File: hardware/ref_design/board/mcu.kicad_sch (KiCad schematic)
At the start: 8 parts, among them U4 RP2354B, X1 12MHz

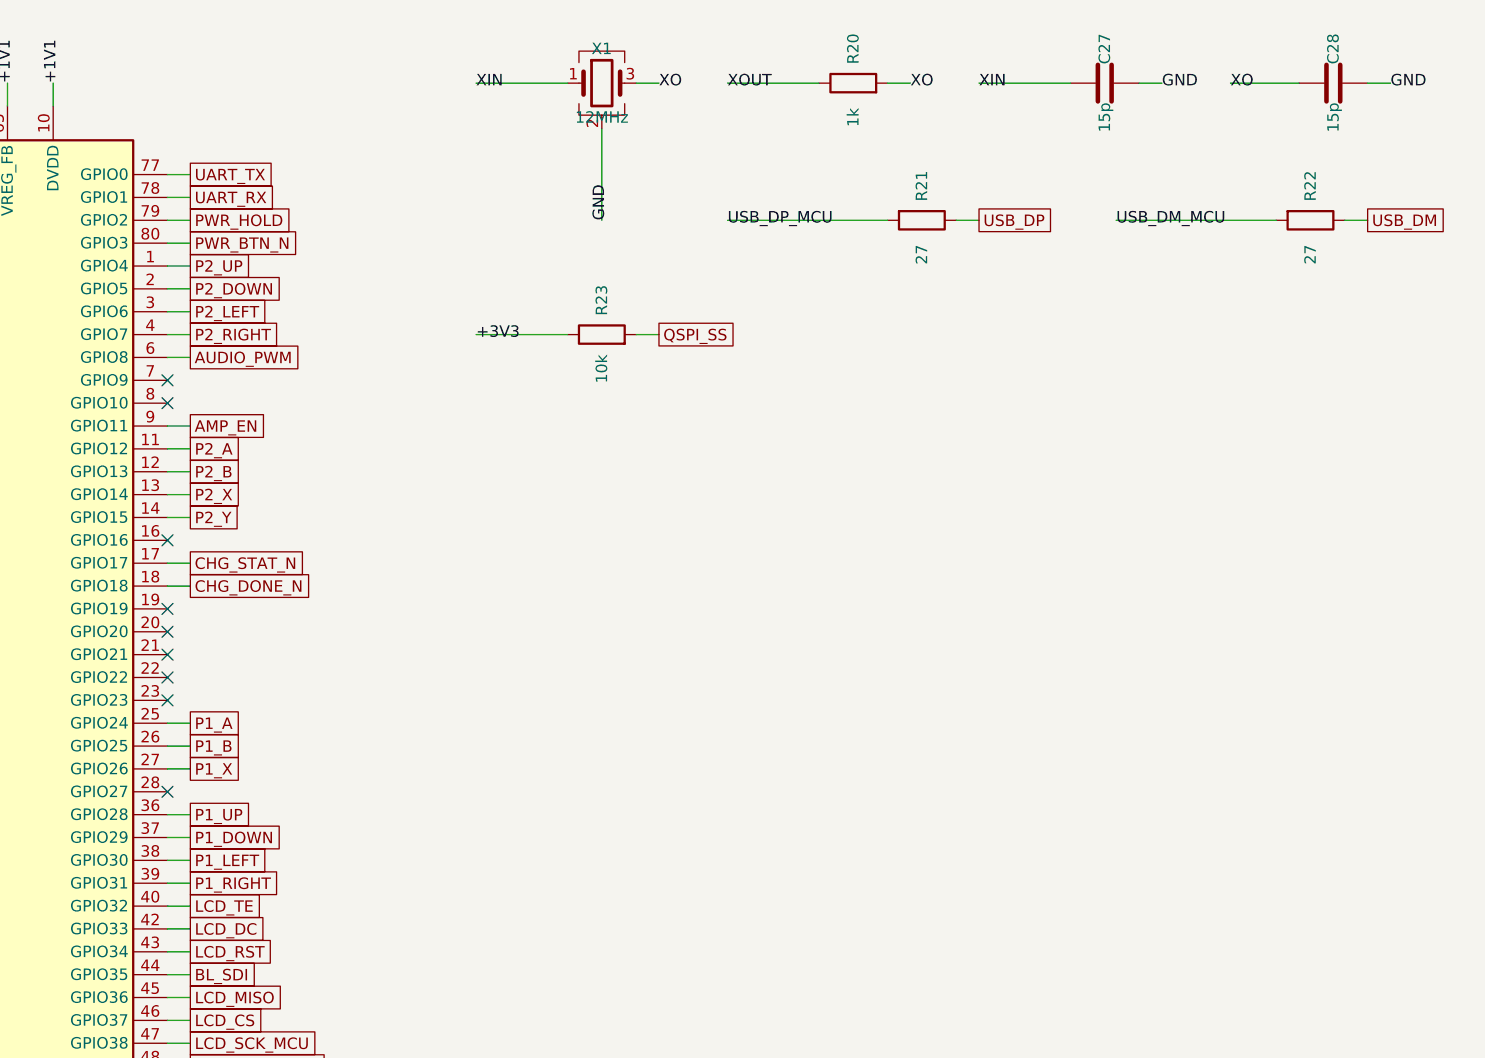
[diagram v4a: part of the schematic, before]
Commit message: 2-layer fork: board, case and docs for the approved cost changes
Board on two layers with every hole >= 0.3 mm (JLC's standard; smaller holes
cost about $40 an order), routed DRC-clean: 0 errors, 0 unconnected, 0 parity.
The RP2354B core is Raspberry Pi's 2-layer layout; its 3V3 pour sits inside
the chip's pads, fenced from the router, and every 3V3 pin stubs into it. GND
is poured on both layers and left out of Freerouting's job; 3V3 is routed.
USB series resistors are 22 ohm 0402 in Raspberry Pi's spots (a 27 ohm 0603
doesn't fit); UART1 on GPIO20/21 and seat 1's right on GPIO23 escape the
crystal's corner. route.py --finish closes what a full run leaves open.

Case 15 mm thick for the 503450 cell; the lid snaps on six hooks, six pins
locate the board; no lens, light pipes or power cap. Fit check: 90 parts, no
collisions. BOM split into factory (about $15.10 a unit) and self-assembled
(about $14-18); assembly, bring-up, pin map and design review updated.

Co-Authored-By: Claude Opus 5.5 <noreply@anthropic.com>
Claude-Session: https://claude.ai/code/session_01KGgEu3CbFtCsvHRQgAFiCN
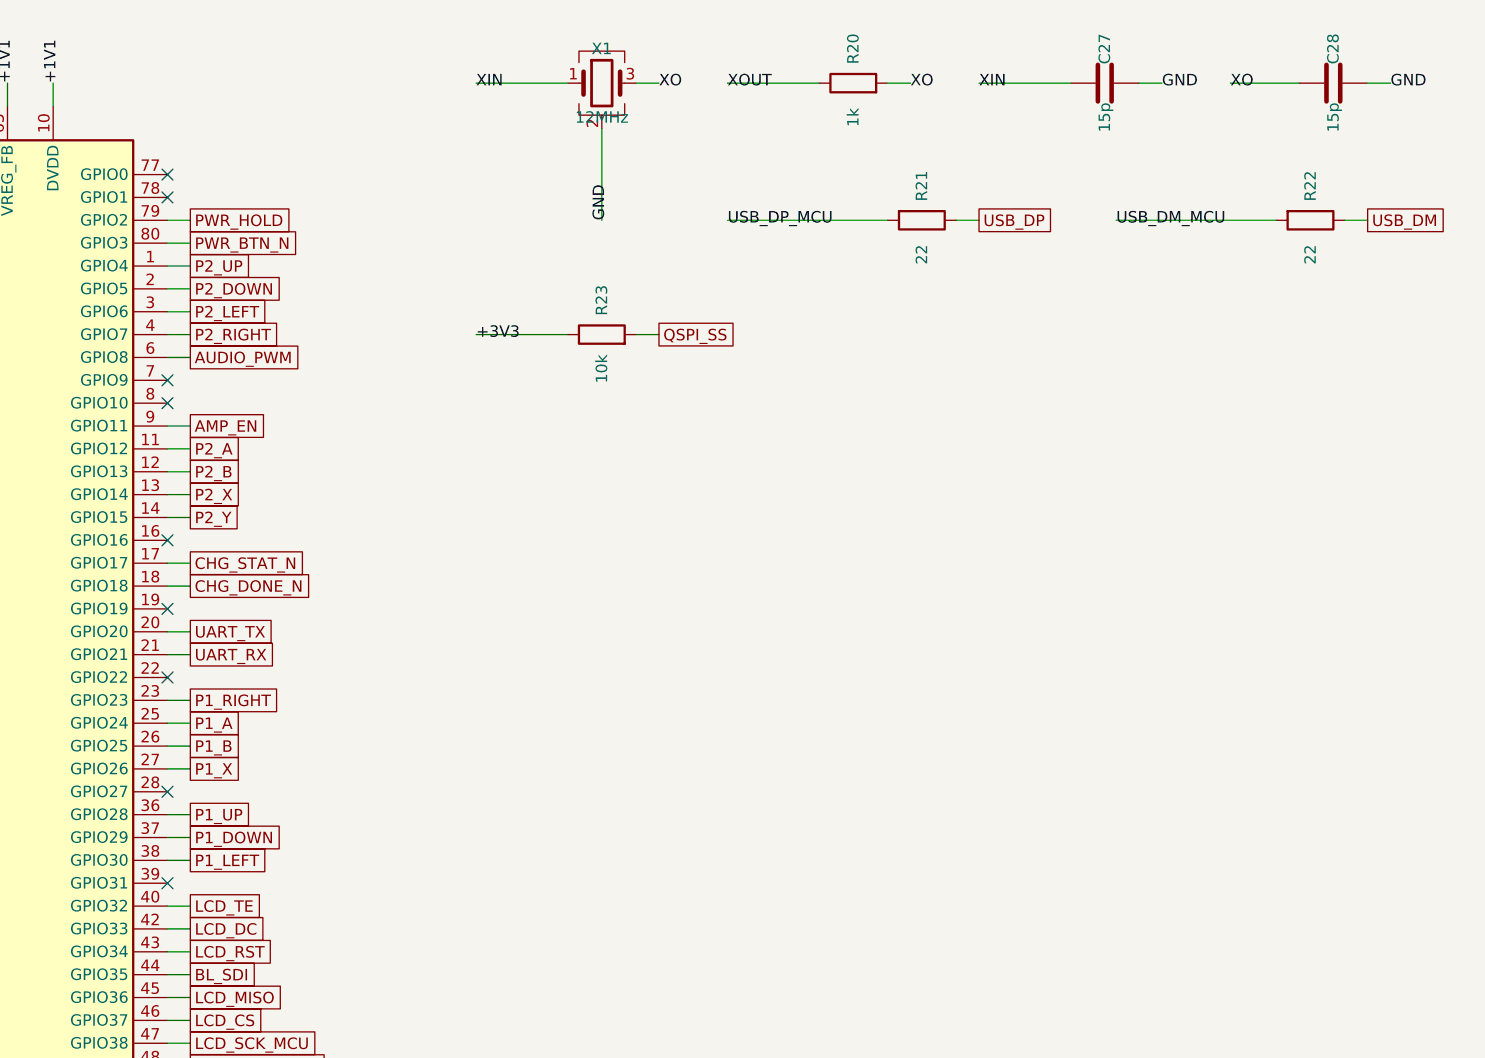
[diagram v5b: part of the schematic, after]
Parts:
- R21, R22: value 27 -> 22; footprint Resistor_SMD:R_0603_1608Metric -> battler:R_0402_1005Metric_RPi; LCSC C25190 -> C25092; MPN 0603WAF270JT5E -> 0402WGF220JTCE
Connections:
- net P1_RIGHT: now also U4.23 (GPIO23); no longer U4.39 (GPIO31)
- net UART_RX: now also U4.21 (GPIO21); no longer U4.78 (GPIO1)
- net UART_TX: now also U4.20 (GPIO20); no longer U4.77 (GPIO0)
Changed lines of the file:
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@@
   (paper "A4")
   (no_connect
+    (at 99.06 45.72)
+)
+  (no_connect
+    (at 99.06 48.26)
+)
+  (no_connect
     (at 99.06 68.58)
 )
@@
 )
   (no_connect
-    (at 99.06 96.52)
-)
-  (no_connect
-    (at 99.06 99.06)
-)
-  (no_connect
     (at 99.06 101.6)
 )
   (no_connect
-    (at 99.06 104.14)
-)
-  (no_connect
     (at 99.06 114.3)
+)
+  (no_connect
+    (at 99.06 124.46)
 )
   (no_connect
@@
   (wire
     (pts
-      (xy 99.06 45.72)
-      (xy 101.6 45.72))
-)
-  (wire
-    (pts
-      (xy 99.06 48.26)
-      (xy 101.6 48.26))
-)
-  (wire
-    (pts
       (xy 99.06 50.8)
       (xy 101.6 50.8))
@@
   (wire
     (pts
+      (xy 99.06 96.52)
+      (xy 101.6 96.52))
+)
+  (wire
+    (pts
+      (xy 99.06 99.06)
+      (xy 101.6 99.06))
+)
+  (wire
+    (pts
       (xy 48.26 99.06)
       (xy 38.1 99.06))
@@
   (wire
     (pts
+      (xy 99.06 104.14)
+      (xy 101.6 104.14))
+)
+  (wire
+    (pts
       (xy 99.06 106.68)
       (xy 101.6 106.68))
@@
       (xy 99.06 121.92)
       (xy 101.6 121.92))
-)
-  (wire
-    (pts
-      (xy 99.06 124.46)
-      (xy 101.6 124.46))
 )
   (wire
@@
     (at 78.74 35.56 90)
 )
+  (global_label "PWR_HOLD"
+    (shape passive)
+    (at 101.6 50.8 0)
+)
+  (global_label "PWR_BTN_N"
+    (shape passive)
+    (at 101.6 53.34 0)
+)
+  (global_label "P2_UP"
+    (shape passive)
+    (at 101.6 55.88 0)
+)
+  (global_label "P2_DOWN"
+    (shape passive)
+    (at 101.6 58.42 0)
+)
+  (global_label "P2_LEFT"
+    (shape passive)
+    (at 101.6 60.96 0)
+)
+  (global_label "P2_RIGHT"
+    (shape passive)
+    (at 101.6 63.5 0)
+)
+  (global_label "AUDIO_PWM"
+    (shape passive)
+    (at 101.6 66.04 0)
+)
+  (global_label "AMP_EN"
+    (shape passive)
+    (at 101.6 73.66 0)
+)
+  (global_label "P2_A"
+    (shape passive)
+    (at 101.6 76.2 0)
+)
+  (global_label "P2_B"
+    (shape passive)
+    (at 101.6 78.74 0)
+)
+  (global_label "P2_X"
+    (shape passive)
+    (at 101.6 81.28 0)
+)
+  (global_label "P2_Y"
+    (shape passive)
+    (at 101.6 83.82 0)
+)
+  (global_label "CHG_STAT_N"
+    (shape passive)
+    (at 101.6 88.9 0)
+)
+  (global_label "CHG_DONE_N"
+    (shape passive)
+    (at 101.6 91.44 0)
+)
   (global_label "UART_TX"
     (shape passive)
-    (at 101.6 45.72 0)
+    (at 101.6 96.52 0)
 )
   (global_label "UART_RX"
     (shape passive)
-    (at 101.6 48.26 0)
-)
-  (global_label "PWR_HOLD"
-    (shape passive)
-    (at 101.6 50.8 0)
-)
-  (global_label "PWR_BTN_N"
-    (shape passive)
-    (at 101.6 53.34 0)
-)
-  (global_label "P2_UP"
-    (shape passive)
-    (at 101.6 55.88 0)
-)
-  (global_label "P2_DOWN"
-    (shape passive)
-    (at 101.6 58.42 0)
-)
-  (global_label "P2_LEFT"
-    (shape passive)
-    (at 101.6 60.96 0)
-)
-  (global_label "P2_RIGHT"
-    (shape passive)
-    (at 101.6 63.5 0)
-)
-  (global_label "AUDIO_PWM"
-    (shape passive)
-    (at 101.6 66.04 0)
-)
-  (global_label "AMP_EN"
-    (shape passive)
-    (at 101.6 73.66 0)
-)
-  (global_label "P2_A"
-    (shape passive)
-    (at 101.6 76.2 0)
-)
-  (global_label "P2_B"
-    (shape passive)
-    (at 101.6 78.74 0)
-)
-  (global_label "P2_X"
-    (shape passive)
-    (at 101.6 81.28 0)
-)
-  (global_label "P2_Y"
-    (shape passive)
-    (at 101.6 83.82 0)
-)
-  (global_label "CHG_STAT_N"
-    (shape passive)
-    (at 101.6 88.9 0)
-)
-  (global_label "CHG_DONE_N"
-    (shape passive)
-    (at 101.6 91.44 0)
+    (at 101.6 99.06 0)
+)
+  (global_label "P1_RIGHT"
+    (shape passive)
+    (at 101.6 104.14 0)
 )
   (global_label "P1_A"
@@
     (shape passive)
     (at 101.6 121.92 0)
-)
-  (global_label "P1_RIGHT"
-    (shape passive)
-    (at 101.6 124.46 0)
 )
   (global_label "LCD_TE"
@@
         (font
           (size 1.27 1.27))))
-    (property "Value" "27"
+    (property "Value" "22"
       (at 182.88 54.61 0)
       (effects
         (font
           (size 1.27 1.27))))
-    (property "Footprint" "Resistor_SMD:R_0603_1608Metric"
+    (property "Footprint" "battler:R_0402_1005Metric_RPi"
       (at 182.88 50.8 0)
       (effects
@@
           (size 1.27 1.27))
         (hide yes)))
-    (property "LCSC" "C25190"
-      (at 0 0 0)
-      (effects
-        (font
-          (size 1.27 1.27))
-        (hide yes)))
-    (property "MPN" "0603WAF270JT5E"
+    (property "LCSC" "C25092"
+      (at 0 0 0)
+      (effects
+        (font
+          (size 1.27 1.27))
+        (hide yes)))
+    (property "MPN" "0402WGF220JTCE"
       (at 0 0 0)
       (effects
@@
         (font
           (size 1.27 1.27))))
-    (property "Value" "27"
+    (property "Value" "22"
       (at 226.06 54.61 0)
       (effects
         (font
           (size 1.27 1.27))))
-    (property "Footprint" "Resistor_SMD:R_0603_1608Metric"
+    (property "Footprint" "battler:R_0402_1005Metric_RPi"
       (at 226.06 50.8 0)
       (effects
@@
           (size 1.27 1.27))
         (hide yes)))
-    (property "LCSC" "C25190"
-      (at 0 0 0)
-      (effects
-        (font
-          (size 1.27 1.27))
-        (hide yes)))
-    (property "MPN" "0603WAF270JT5E"
-      (at 0 0 0)
-      (effects
+    (property "LCSC" "C25092"
+      (at 0 0 0)
+      (effects
+        (font
+          (size 1.27 1.27))
+        (hide yes)))
+    (property "MPN" "0402WGF220JTCE"
+      (at 0 0 0)
+      (effects

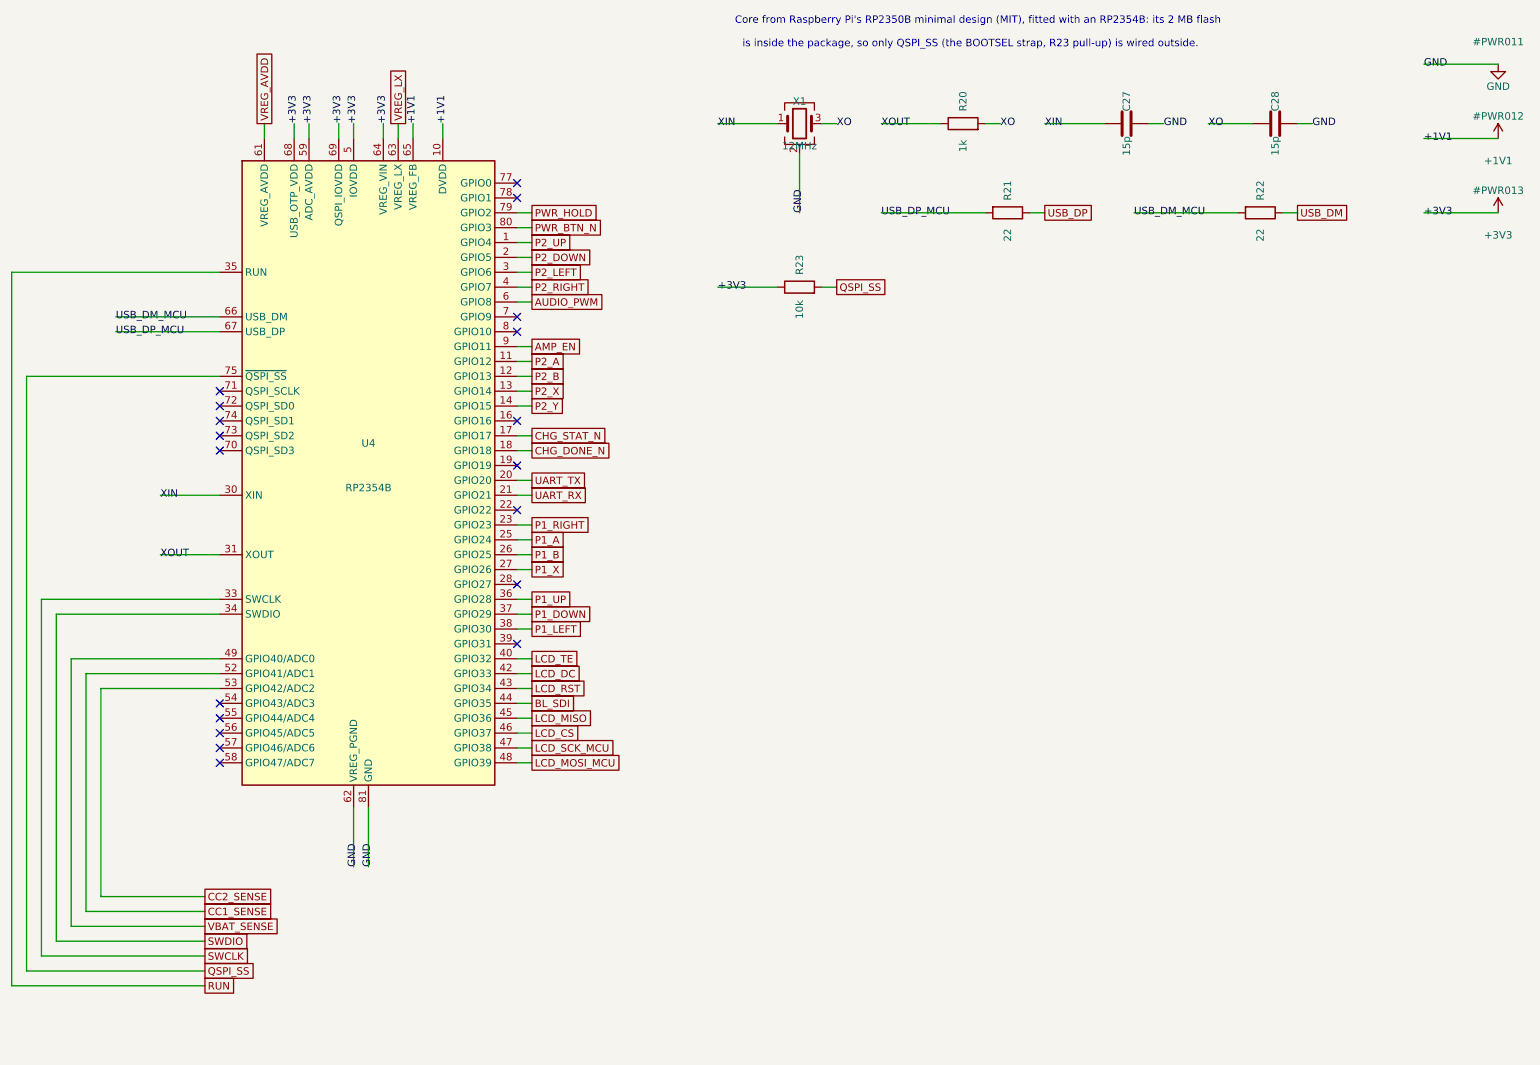
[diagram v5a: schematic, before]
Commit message: Reference design: plug-in ER-TFT035IPS-6 panel, pins and pin escapes for 2 layers
- Panel: EastRising ER-TFT035IPS-6 (ILI9488, 320x480 IPS) on a Hirose FH12-50S
  ZIF connector (J3) that JLC places, instead of the QD3525's hand-soldered tail.
  Case panel/FPC geometry, fit check (FPC zones), backlight sinks paired onto
  its two cathode pins, docs and BOM updated. Prices from both shops' carts:
  about $14.20 a unit at 10 with shipping.
- Pins reassigned for two layers: each faces where its net goes, in fan-out
  order (seat 1's face buttons, panel reset, backlight and ADC inputs on
  GPIO40-47; seat 1's cross and the panel's TE on GPIO28-32).
- build_pcb.copy_escapes: Raspberry Pi's own routing out of the RP2354B's pins,
  copied with the core and locked, so no pin gets boxed in by its neighbours.
  The board now routes completely in about 10 minutes.
- route.py: loose tracks are trimmed back to their last real join instead of
  deleted (Freerouting meets stubs part-way along), T-joins are split and
  duplicate tracks dropped; Freerouting routes to +5 um clearance and a 0.12 mm
  inset outline (it rounded under 0.15 mm and hugged the board edge).
- MCU sheet region widened for the longer labels; datasheet list updated for
  the 2-layer parts; old panel landing footprint/tool and the unused side
  switch footprint removed.

Checks: netlist PASS (122 parts, 115 nets), ERC 0, DRC 0 errors / 0
unconnected / 0 parity (2 cosmetic silk warnings), holes 0.3/0.6/0.65/2.2 mm,
fit PASS on 91 parts.

Co-Authored-By: Claude Opus 5.5 <noreply@anthropic.com>
Claude-Session: https://claude.ai/code/session_01KGgEu3CbFtCsvHRQgAFiCN
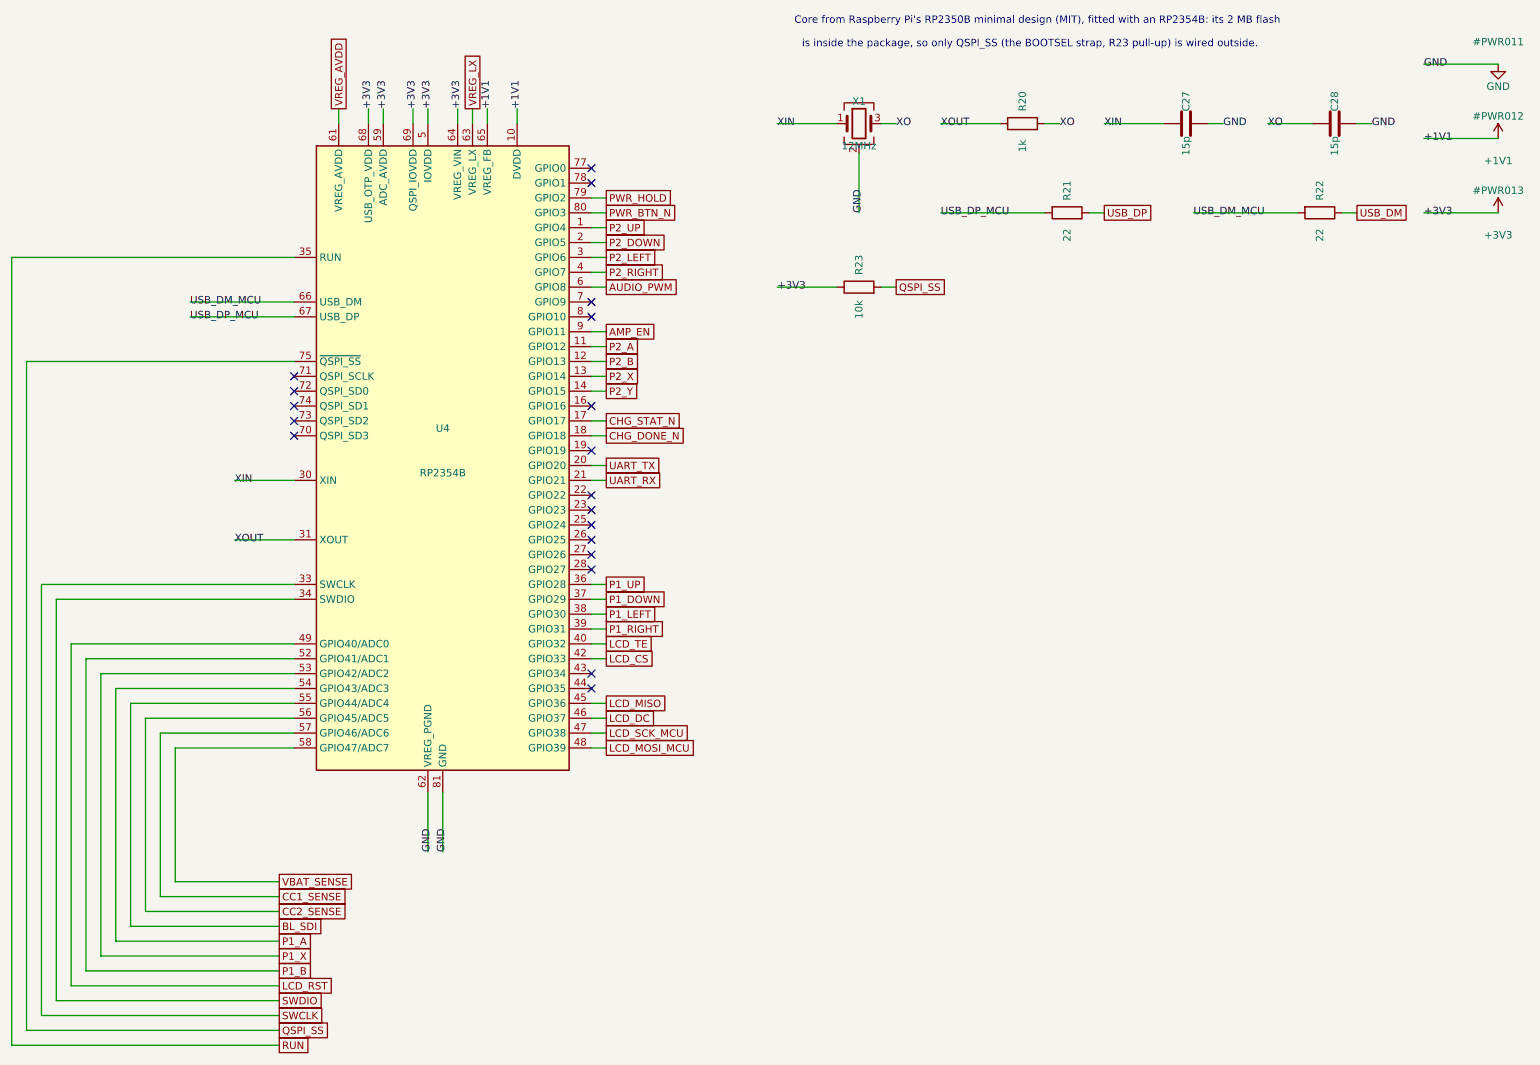
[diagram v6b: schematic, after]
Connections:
- net BL_SDI: now also U4.55 (GPIO44/ADC4); no longer U4.44 (GPIO35)
- net CC1_SENSE: now also U4.57 (GPIO46/ADC6); no longer U4.52 (GPIO41/ADC1)
- net CC2_SENSE: now also U4.56 (GPIO45/ADC5); no longer U4.53 (GPIO42/ADC2)
- net LCD_CS: now also U4.42 (GPIO33); no longer U4.46 (GPIO37)
- net LCD_DC: now also U4.46 (GPIO37); no longer U4.42 (GPIO33)
- net LCD_RST: now also U4.49 (GPIO40/ADC0); no longer U4.43 (GPIO34)
- net P1_A: now also U4.54 (GPIO43/ADC3); no longer U4.25 (GPIO24)
- net P1_B: now also U4.52 (GPIO41/ADC1); no longer U4.26 (GPIO25)
- net P1_RIGHT: now also U4.39 (GPIO31); no longer U4.23 (GPIO23)
- net P1_X: now also U4.53 (GPIO42/ADC2); no longer U4.27 (GPIO26)
- net VBAT_SENSE: now also U4.58 (GPIO47/ADC7); no longer U4.49 (GPIO40/ADC0)
